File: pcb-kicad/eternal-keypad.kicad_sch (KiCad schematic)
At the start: 81 parts

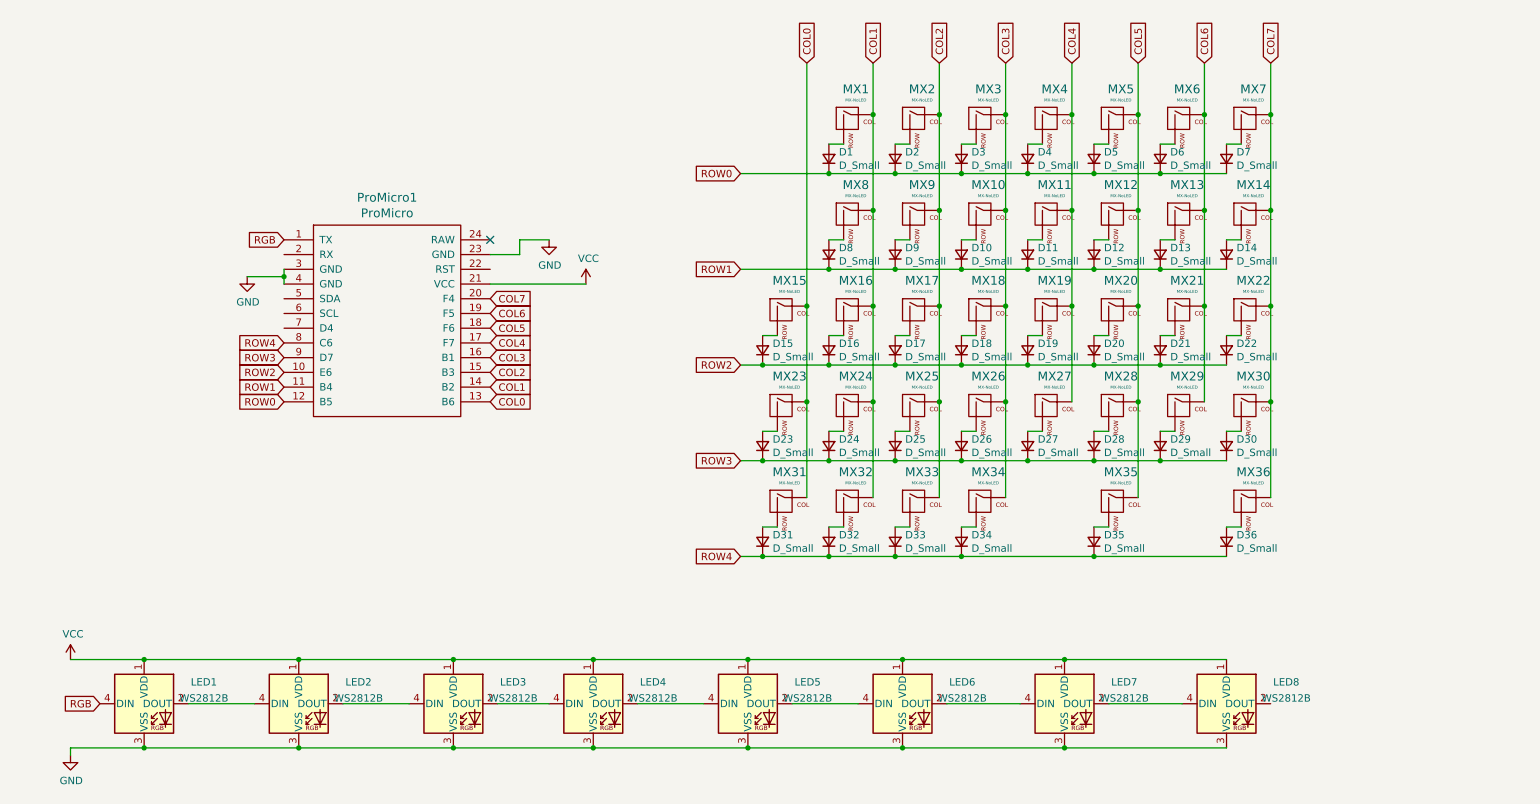
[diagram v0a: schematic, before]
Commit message: Add power, reset, RGB Cutoff, Battery Pads
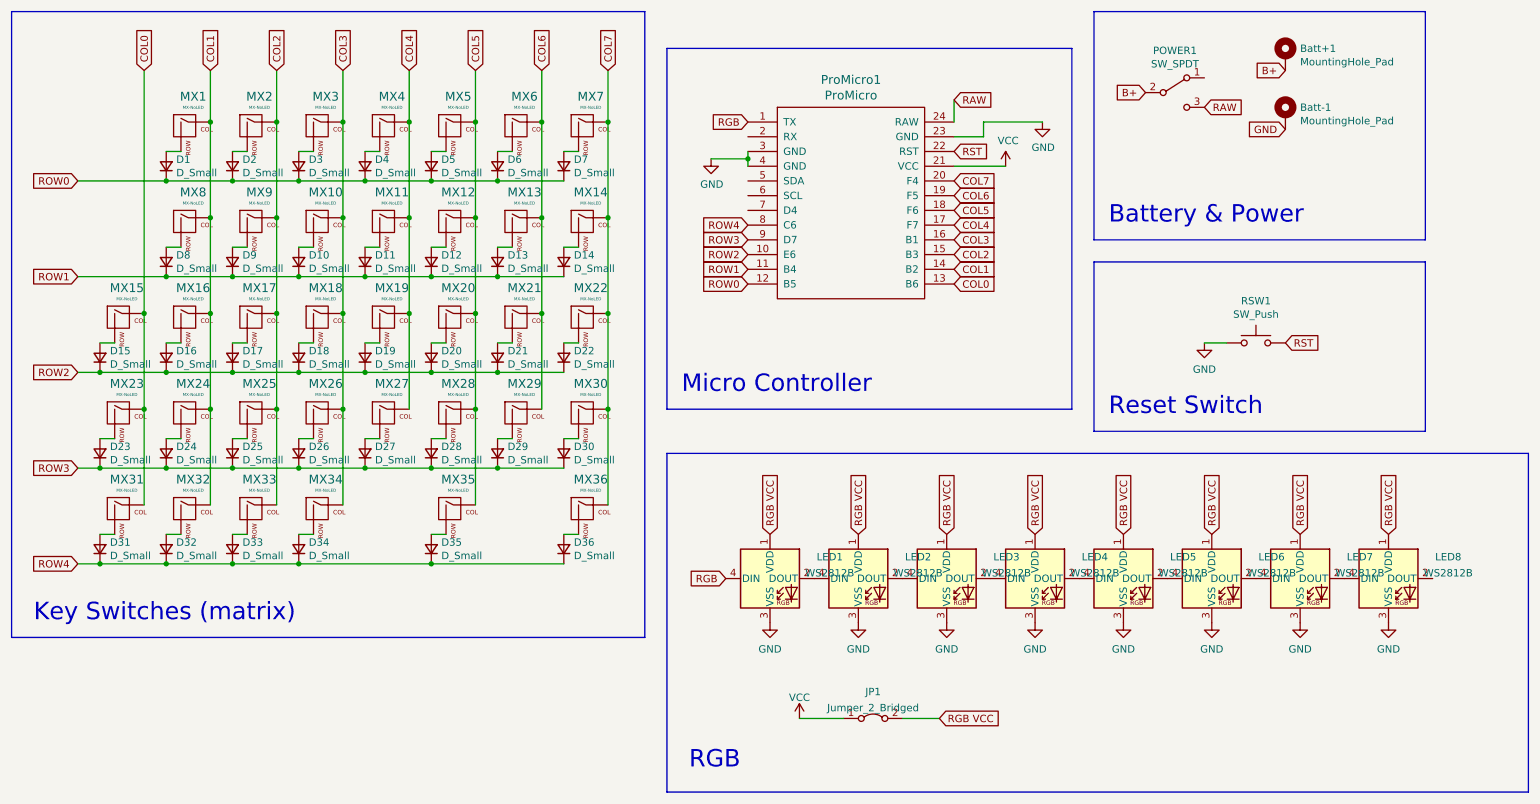
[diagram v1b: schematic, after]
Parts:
- added Batt+1, Batt-1: MountingHole_Pad, * duckyb-collection:1pin_conn, symbol Mechanical:MountingHole_Pad
- added JP1: Jumper_2_Bridged, Jumper:SolderJumper-2_P1.3mm_Bridged2Bar_RoundedPad1.0x1.5mm, symbol Jumper:Jumper_2_Bridged
- added POWER1: SW_SPDT, * duckyb-collection:SPDT_C128955, symbol Switch:SW_SPDT
- added RSW1: SW_Push, * duckyb-collection:Tactile-Switch_SMT, symbol Switch:SW_Push
- LED1, LED2, LED3, LED4, LED5, LED6, LED7, LED8: footprint LED_SMD:LED_WS2812B_PLCC4_5.0x5.0mm_P3.2mm -> * duckyb-collection:LED_WS2812B_PLCC4_5.0x5.0mm_P3.2mm
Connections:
- net GND: now also Batt-1.1, RSW1.1
- net VCC: now also JP1.1 (A); no longer LED1.1 (VDD), LED2.1 (VDD), LED3.1 (VDD), LED4.1 (VDD), LED5.1 (VDD), LED6.1 (VDD), LED7.1 (VDD), LED8.1 (VDD)
- net RST: now reaches ProMicro1.22 (RST)
- net RST: now also RSW1.2
- net RAW: now reaches ProMicro1.24 (RAW)
- net RAW: now also POWER1.3 (C)
- new net B+: Batt+1.1, POWER1.2 (B)
- new net RGB VCC: JP1.2 (B), LED1.1 (VDD), LED2.1 (VDD), LED3.1 (VDD), LED4.1 (VDD), LED5.1 (VDD), LED6.1 (VDD), LED7.1 (VDD), LED8.1 (VDD)
- no-connect marks 1 -> 0
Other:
- note added: "Battery & Power"
- note added: "Key Switches (matrix)"
- note added: "Micro Controller"
- note added: "RGB"
- note added: "Reset Switch"
- title: (none) -> Eternal Keypad
- moved on the sheet: D1, D10, D11, D12, D13, D14, D15, D16, D17, D18, D19, D2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
